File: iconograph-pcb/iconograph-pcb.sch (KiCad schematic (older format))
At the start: 36 parts, among them J1 Conn_01x02, J10 Conn_01x07, J11 Conn_01x04, J12 Conn_01x04, J13 Conn_01x04, J2 Conn_01x03, J3 Anderson_two_redblack_src, J4 Conn_01x02, J5 Conn_01x03, J6 Conn_01x02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

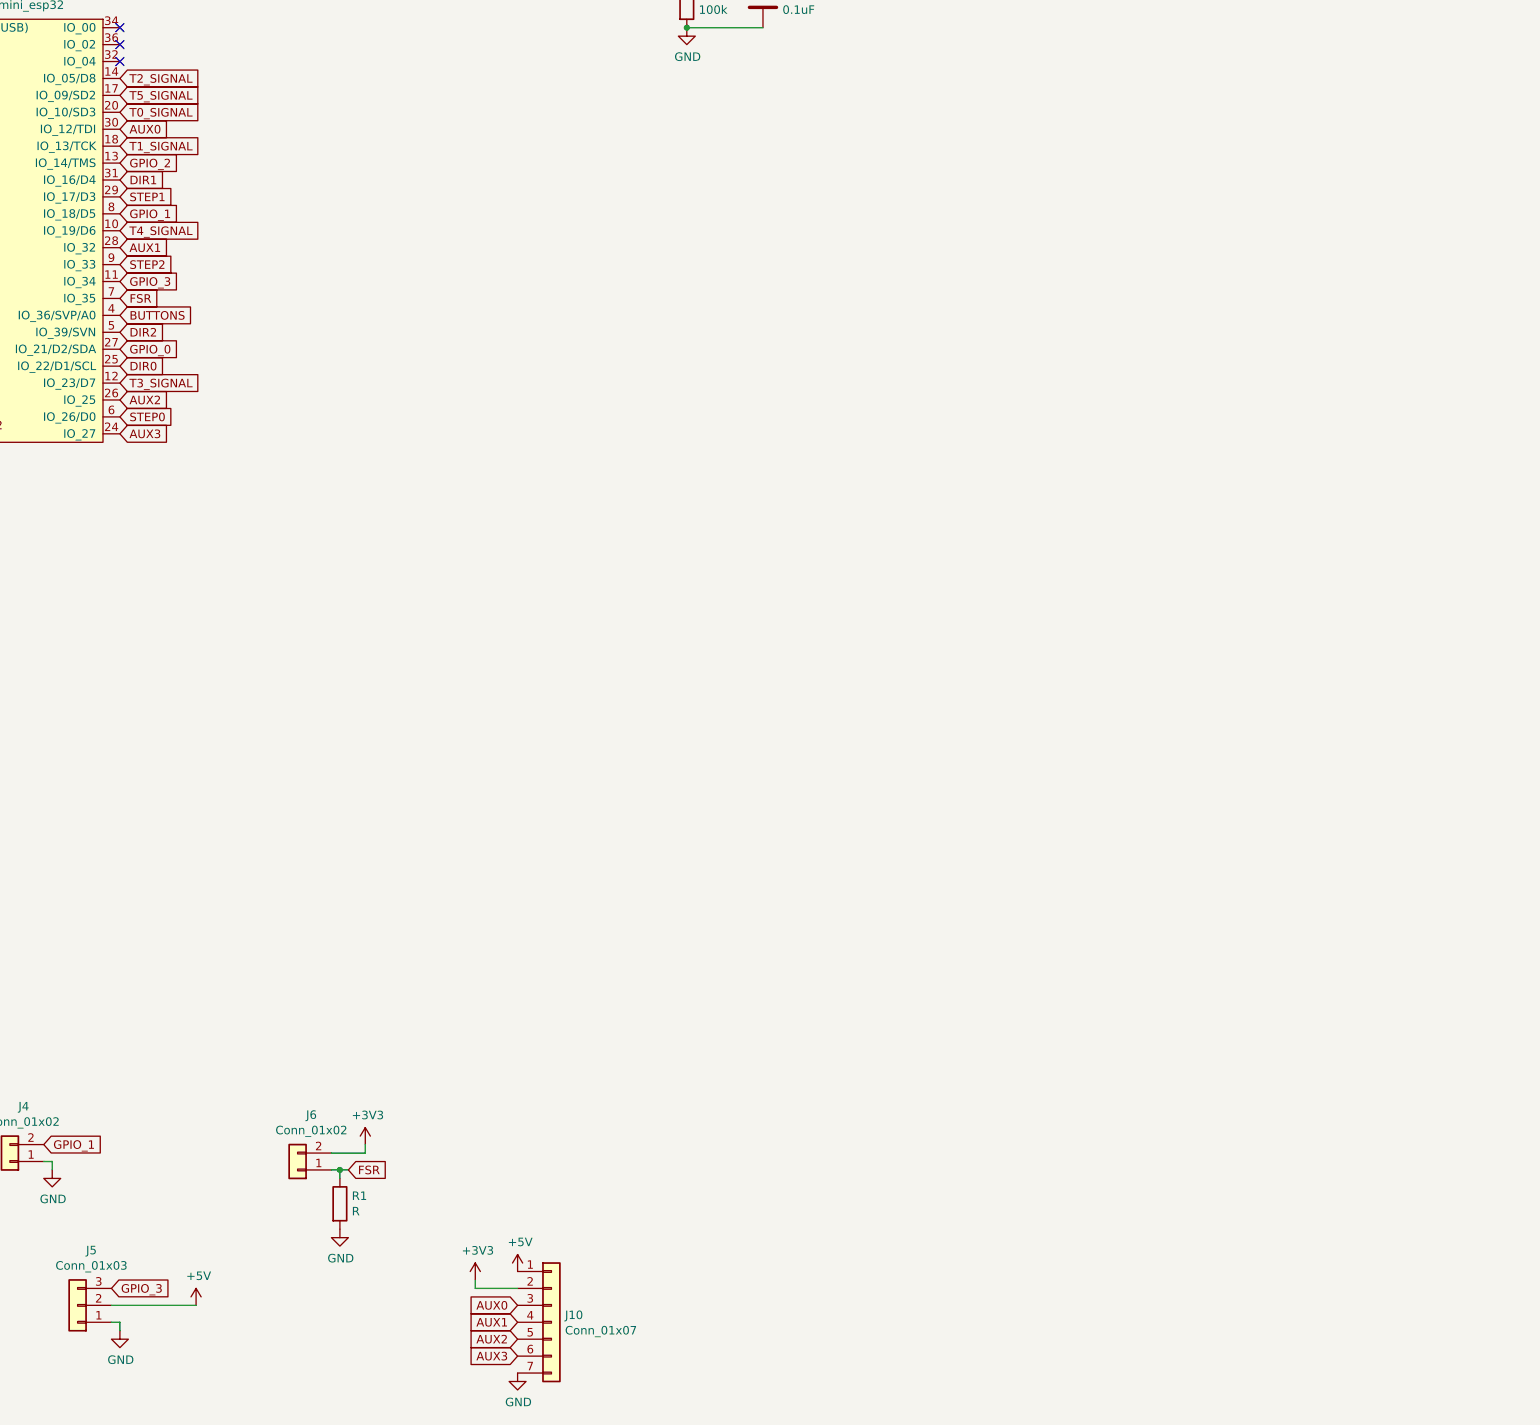
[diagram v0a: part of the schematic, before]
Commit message: Add micro sd holder
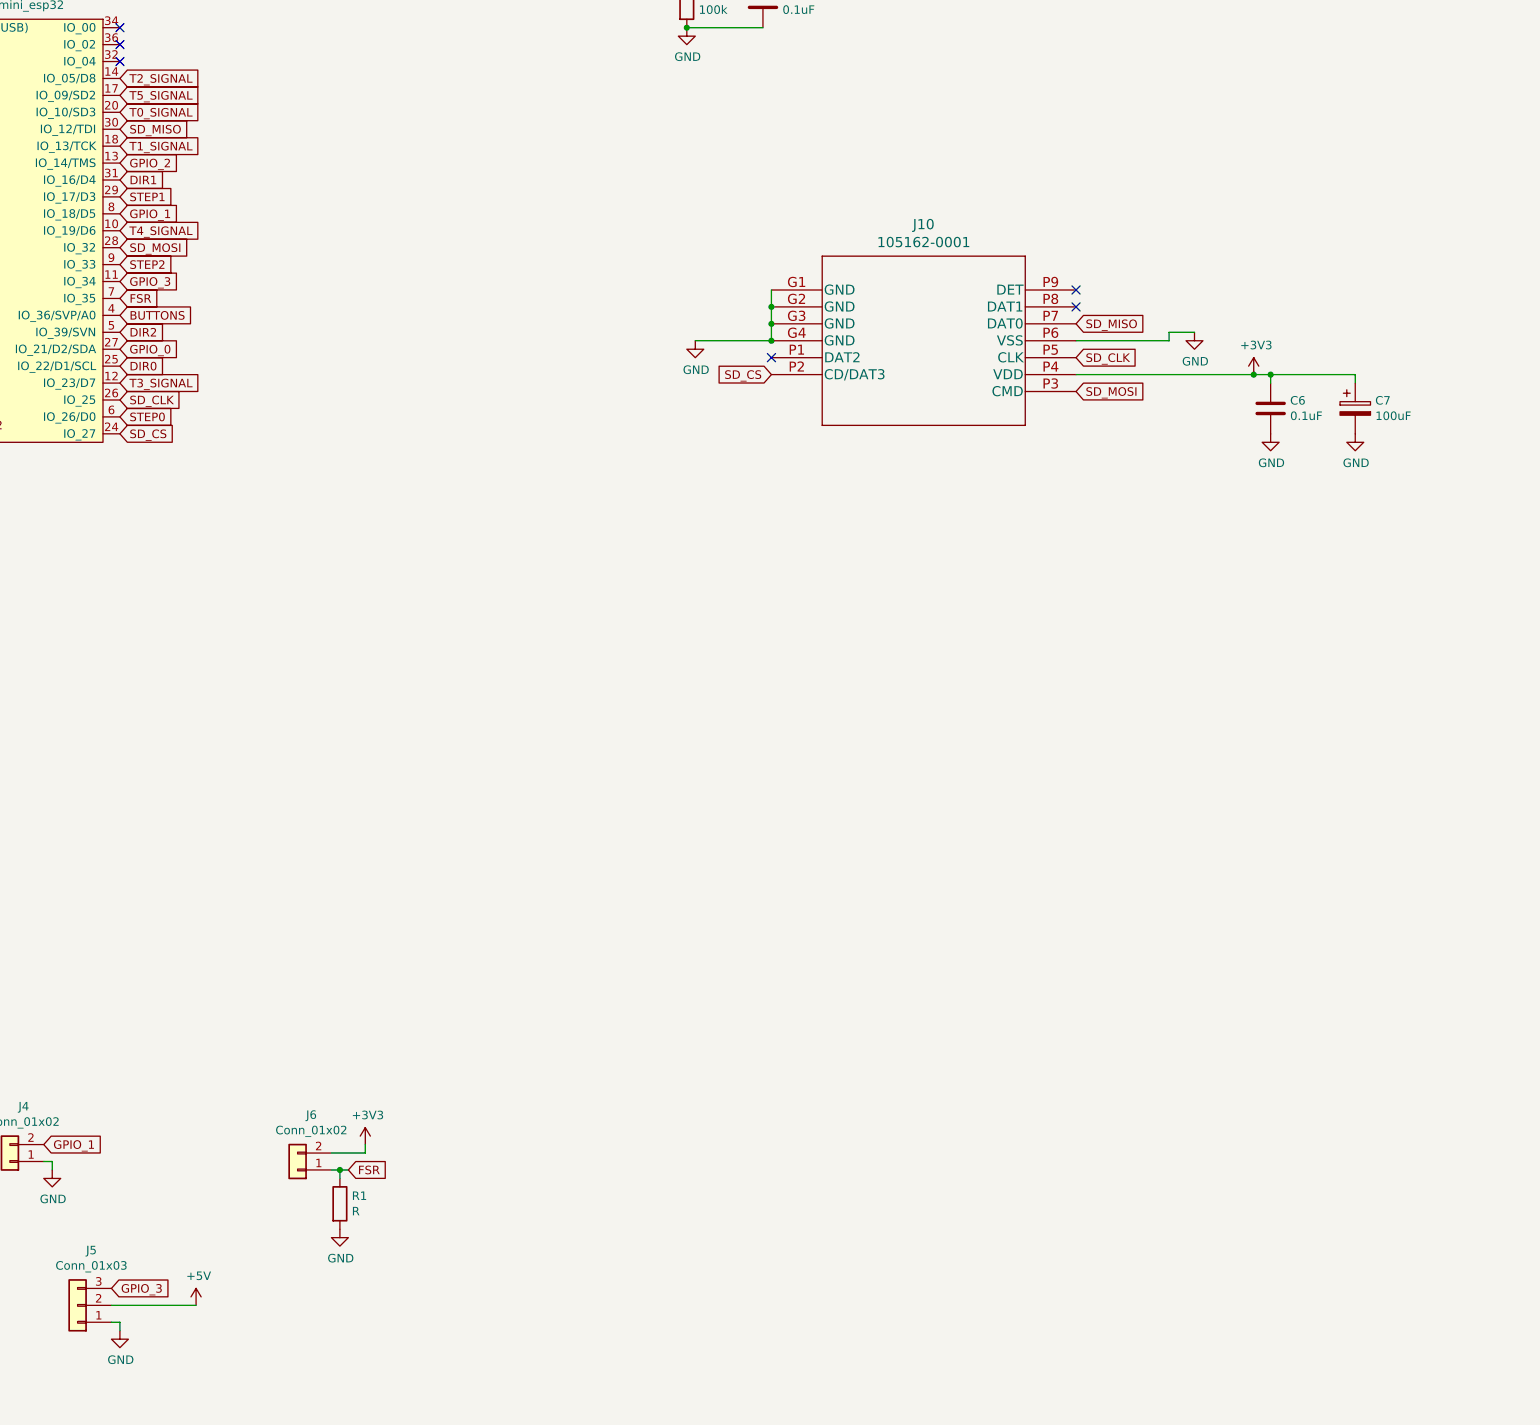
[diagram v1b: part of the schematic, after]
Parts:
- removed J10: Conn_01x07, symbol Connector_Generic:Conn_01x07
- added C6: 0.1uF, symbol Device:C
- added C7: 100uF, symbol Device:CP
- added J10: 105162-0001, snapeda:105162-0001, symbol snapeda-1051620001:105162-0001
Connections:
- net +3V3: now also C6.1, C7.1, J10.P4 (VDD)
- net GND: now also C6.2, C7.2, J10.G1 (GND), J10.G2 (GND), J10.G3 (GND), J10.G4 (GND), J10.P6 (VSS)
- net AUX0 renamed SD_MISO
- net SD_MISO: now also J10.P7 (DAT0)
- net AUX1 renamed SD_MOSI
- net SD_MOSI: now also J10.P3 (CMD)
- net AUX2 renamed SD_CLK
- net SD_CLK: now also J10.P5 (CLK)
- net AUX3 renamed SD_CS
- net SD_CS: now also J10.P2 (CD/DAT3)
- no-connect marks 17 -> 20
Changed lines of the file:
@@
 Text GLabel 2350 4550 2    50   Input ~ 0
 DIR2
-Text GLabel 2350 3350 2    50   Input ~ 0
-AUX0
-Text GLabel 2350 4050 2    50   Input ~ 0
-AUX1
-Text GLabel 2350 4950 2    50   Input ~ 0
-AUX2
-Text GLabel 2350 5150 2    50   Input ~ 0
-AUX3
-$Comp
-L Connector_Generic:Conn_01x07 J10
-U 1 1 5FEEC6E1
-P 4900 10400
-F 0 "J10" H 4980 10442 50  0000 L CNN
-F 1 "Conn_01x07" H 4980 10351 50  0000 L CNN
-F 2 "" H 4900 10400 50  0001 C CNN
-F 3 "~" H 4900 10400 50  0001 C CNN
-	1    4900 10400
-	1    0    0    -1
-$EndComp
-$Comp
-L power:+5V #PWR026
-U 1 1 5FEF28EC
-P 4700 10100
-F 0 "#PWR026" H 4700 9950 50  0001 C CNN
-F 1 "+5V" H 4715 10273 50  0000 C CNN
-F 2 "" H 4700 10100 50  0001 C CNN
-F 3 "" H 4700 10100 50  0001 C CNN
-	1    4700 10100
-	1    0    0    -1
-$EndComp
-$Comp
-L power:+3V3 #PWR024
-U 1 1 5FEF92B4
-P 4450 10150
-F 0 "#PWR024" H 4450 10000 50  0001 C CNN
-F 1 "+3V3" H 4465 10323 50  0000 C CNN
-F 2 "" H 4450 10150 50  0001 C CNN
-F 3 "" H 4450 10150 50  0001 C CNN
-	1    4450 10150
-	1    0    0    -1
-$EndComp
-Wire Wire Line
-	4450 10150 4450 10200
-Wire Wire Line
-	4450 10200 4700 10200
-Text GLabel 4700 10300 0    50   Input ~ 0
-AUX0
-Text GLabel 4700 10400 0    50   Input ~ 0
-AUX1
-Text GLabel 4700 10500 0    50   Input ~ 0
-AUX2
-Text GLabel 4700 10600 0    50   Input ~ 0
-AUX3
-$Comp
-L power:GND #PWR027
-U 1 1 5FF01213
-P 4700 10700
-F 0 "#PWR027" H 4700 10450 50  0001 C CNN
-F 1 "GND" H 4705 10527 50  0000 C CNN
-F 2 "" H 4700 10700 50  0001 C CNN
-F 3 "" H 4700 10700 50  0001 C CNN
-	1    4700 10700
-	1    0    0    -1
-$EndComp
 NoConn ~ 2350 2750
 NoConn ~ 2350 2850
@@
 Wire Wire Line
 	5700 1900 5700 2350
+$Comp
+L power:GND #PWR024
+U 1 1 5FDCAA90
+P 5750 4600
+F 0 "#PWR024" H 5750 4350 50  0001 C CNN
+F 1 "GND" H 5755 4427 50  0000 C CNN
+F 2 "" H 5750 4600 50  0001 C CNN
+F 3 "" H 5750 4600 50  0001 C CNN
+	1    5750 4600
+	1    0    0    -1
+$EndComp
+$Comp
+L power:+3V3 #PWR027
+U 1 1 5FDD2807
+P 9050 4800
+F 0 "#PWR027" H 9050 4650 50  0001 C CNN
+F 1 "+3V3" H 9065 4973 50  0000 C CNN
+F 2 "" H 9050 4800 50  0001 C CNN
+F 3 "" H 9050 4800 50  0001 C CNN
+	1    9050 4800
+	1    0    0    -1
+$EndComp
+Text GLabel 8000 4700 2    50   Input ~ 0
+SD_CLK
+Text GLabel 8000 4900 2    50   Input ~ 0
+SD_MOSI
+Text GLabel 8000 4500 2    50   Input ~ 0
+SD_MISO
+Text GLabel 6200 4800 0    50   Input ~ 0
+SD_CS
+$Comp
+L snapeda-1051620001:105162-0001 J10
+U 1 1 5FDDDB50
+P 6200 4300
+F 0 "J10" H 7100 4687 60  0000 C CNN
+F 1 "105162-0001" H 7100 4581 60  0000 C CNN
+F 2 "snapeda:105162-0001" H 7100 4540 60  0001 C CNN
+F 3 "" H 6200 4300 60  0000 C CNN
+	1    6200 4300
+	1    0    0    -1
+$EndComp
+Wire Wire Line
+	5750 4600 6200 4600
+Wire Wire Line
+	6200 4600 6200 4500
+Connection ~ 6200 4600
+Wire Wire Line
+	6200 4500 6200 4400
+Connection ~ 6200 4500
+Wire Wire Line
+	6200 4400 6200 4300
+Connection ~ 6200 4400
+$Comp
+L power:GND #PWR026
+U 1 1 5FE0179B
+P 8700 4550
+F 0 "#PWR026" H 8700 4300 50  0001 C CNN
+F 1 "GND" H 8705 4377 50  0000 C CNN
+F 2 "" H 8700 4550 50  0001 C CNN
+F 3 "" H 8700 4550 50  0001 C CNN
+	1    8700 4550
+	1    0    0    -1
+$EndComp
+Wire Wire Line
+	8000 4800 9050 4800
+Wire Wire Line
+	8700 4550 8550 4550
+Wire Wire Line
+	8550 4550 8550 4600
+Wire Wire Line
+	8550 4600 8000 4600
+NoConn ~ 8000 4400
+NoConn ~ 6200 4700
+Text GLabel 2350 3350 2    50   Input ~ 0
+SD_MISO
+Text GLabel 2350 4050 2    50   Input ~ 0
+SD_MOSI
+Text GLabel 2350 4950 2    50   Input ~ 0
+SD_CLK
+Text GLabel 2350 5150 2    50   Input ~ 0
+SD_CS
+NoConn ~ 8000 4300
+$Comp
+L Device:C C6
+U 1 1 5FE4A609
+P 9150 5000
+F 0 "C6" H 9265 5046 50  0000 L CNN
+F 1 "0.1uF" H 9265 4955 50  0000 L CNN
+F 2 "" H 9188 4850 50  0001 C CNN
+F 3 "~" H 9150 5000 50  0001 C CNN
+	1    9150 5000
+	1    0    0    -1
+$EndComp
+$Comp
+L Device:CP C7
+U 1 1 5FE4B3F3
+P 9650 5000
+F 0 "C7" H 9768 5046 50  0000 L CNN
+F 1 "100uF" H 9768 4955 50  0000 L CNN
+F 2 "" H 9688 4850 50  0001 C CNN
+F 3 "~" H 9650 5000 50  0001 C CNN
+	1    9650 5000
+	1    0    0    -1
+$EndComp
+Wire Wire Line
+	9050 4800 9150 4800
+Wire Wire Line
+	9650 4800 9650 4850
+Connection ~ 9050 4800
+Wire Wire Line
+	9150 4850 9150 4800
+Connection ~ 9150 4800
+Wire Wire Line
+	9150 4800 9650 4800
+$Comp
+L power:GND #PWR040
+U 1 1 5FE5D28A
+P 9150 5150
+F 0 "#PWR040" H 9150 4900 50  0001 C CNN
+F 1 "GND" H 9155 4977 50  0000 C CNN
+F 2 "" H 9150 5150 50  0001 C CNN
+F 3 "" H 9150 5150 50  0001 C CNN
+	1    9150 5150
+	1    0    0    -1
+$EndComp
+$Comp
+L power:GND #PWR041
+U 1 1 5FE5D577
+P 9650 5150
+F 0 "#PWR041" H 9650 4900 50  0001 C CNN
+F 1 "GND" H 9655 4977 50  0000 C CNN
+F 2 "" H 9650 5150 50  0001 C CNN
+F 3 "" H 9650 5150 50  0001 C CNN
+	1    9650 5150
+	1    0    0    -1
+$EndComp
 $EndSCHEMATC

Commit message: PCB v1.0
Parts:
- added D1: D_TVS, Diode_THT:D_DO-15_P10.16mm_Horizontal, symbol Device:D_TVS
- added H1, H2, H3, H4: MountingHole, MountingHole:MountingHole_3.2mm_M3, symbol Mechanical:MountingHole
- added J14: Conn_01x03, homebrew:Wurth_ScrewTerminal_1x03_P5.00mm_691137710003, symbol Connector_Generic:Conn_01x03
- C1, C2, C3, C4, C7: footprint (none) -> Capacitor_THT:CP_Radial_D8.0mm_P3.50mm
- C5, C6: footprint (none) -> Capacitor_THT:C_Disc_D5.1mm_W3.2mm_P5.00mm
- J1, J4, J6, J8, J9: footprint (none) -> homebrew:Wurth_ScrewTerminal_1x02_P5.00mm_691137710002
- J11, J12, J13: footprint (none) -> Connector_PinHeader_2.54mm:PinHeader_1x04_P2.54mm_Vertical
- J2, J5: footprint (none) -> homebrew:Wurth_ScrewTerminal_1x03_P5.00mm_691137710003
- J3: footprint (none) -> homebrew:Anderson_1336G1_right_angle_bottom_two
- J7: footprint (none) -> Connector_PinHeader_2.54mm:PinHeader_1x05_P2.54mm_Vertical
- R1: value R -> 22k; footprint (none) -> Resistor_THT:R_Axial_DIN0207_L6.3mm_D2.5mm_P7.62mm_Horizontal
- R2, R3, R4, R5, R6: footprint (none) -> Resistor_THT:R_Axial_DIN0207_L6.3mm_D2.5mm_P7.62mm_Horizontal
- SW1, SW2, SW3: footprint (none) -> Button_Switch_THT:SW_DIP_SPSTx03_Slide_9.78x9.8mm_W7.62mm_P2.54mm
- SW4, SW5, SW6, SW7: footprint (none) -> snapeda:SW_1825910-6-4
- U1: footprint (none) -> snapeda:ESP32_mini
- U2: footprint (none) -> Package_DIP:DIP-16_W7.62mm
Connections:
- net +3V3: now also J14.2 (Pin_2)
- net +5V: now also J14.3 (Pin_3)
- net GND: now also D1.2 (A2), J14.1 (Pin_1)
- net GPIO_0: now also U1.13 (IO_14/TMS); no longer U1.27 (IO_21/D2/SDA)
- net GPIO_2: now also U1.27 (IO_21/D2/SDA); no longer U1.13 (IO_14/TMS)
- net T1_SIGNAL: now also U1.10 (IO_19/D6); no longer U1.18 (IO_13/TCK)
- net T2_SIGNAL: now also U1.12 (IO_23/D7); no longer U1.14 (IO_05/D8)
- net T3_SIGNAL: now also U1.14 (IO_05/D8); no longer U1.12 (IO_23/D7)
- net T4_SIGNAL: now also U1.18 (IO_13/TCK); no longer U1.10 (IO_19/D6)
- net VCC: now also D1.1 (A1)
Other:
- note added: "microSD card"
- moved on the sheet: C6, C7, J10
